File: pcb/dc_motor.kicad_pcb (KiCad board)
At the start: 2 copper layers, 0 parts

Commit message: Sch complete.
first revision.
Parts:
- added C1: 100nF, Capacitor_SMD:C_0603_1608Metric, F.Cu at (147.3, 112.8)
- added C10: 220nF, Capacitor_SMD:C_0603_1608Metric, F.Cu at (143.3, 112.9)
- added C11: 220nF, Capacitor_SMD:C_0603_1608Metric, F.Cu at (146.3, 110.3)
- added C12: 100nF, Capacitor_SMD:C_0603_1608Metric, F.Cu at (175.5, 81.0)
- added C13: 220nF, Capacitor_SMD:C_0603_1608Metric, F.Cu at (171.4, 83.6)
- added C14: 100nF, Capacitor_SMD:C_0603_1608Metric, F.Cu at (143.3, 115.4)
- added C15: 220nF, Capacitor_SMD:C_0603_1608Metric, F.Cu at (172.5, 86.1)
- added C16: 220nF, Capacitor_SMD:C_0603_1608Metric, F.Cu at (175.4, 83.6)
- added C17: 100nF, Capacitor_SMD:C_0603_1608Metric, F.Cu at (155.3, 112.0)
- added C18: 220nF, Capacitor_SMD:C_0603_1608Metric, F.Cu at (139.3, 114.4)
- added C19: 100nF, Capacitor_SMD:C_0603_1608Metric, F.Cu at (147.3, 115.3)
- added C2: 100nF, Capacitor_SMD:C_0603_1608Metric, F.Cu at (176.5, 91.2)
- added C20: 100nF, Capacitor_SMD:C_0603_1608Metric, F.Cu at (179.4, 83.5)
- added C3: 100nF, Capacitor_SMD:C_0603_1608Metric, F.Cu at (164.9, 102.8)
- added C4: 100nF, Capacitor_SMD:C_0603_1608Metric, F.Cu at (168.9, 100.3)
- added C5: 100nF, Capacitor_SMD:C_0603_1608Metric, F.Cu at (173.5, 97.3)
- added C6: 100nF, Capacitor_SMD:C_0603_1608Metric, F.Cu at (151.3, 114.0)
- added C7: 10uF, Capacitor_SMD:C_0805_2012Metric, F.Cu at (165.7, 95.0)
- added C8: 10uF, Capacitor_SMD:C_0805_2012Metric, F.Cu at (171.6, 78.3)
- added C9: 1000uF/35V, Capacitor_THT:CP_Radial_D10.0mm_P5.00mm, F.Cu at (148.1, 94.9)
- added D1: 10V, Diode_SMD:D_SOD-123, F.Cu at (134.4, 114.8)
- added D2: Power, LED_SMD:LED_0603_1608Metric, F.Cu at (142.2, 110.3)
- added D3: RIGTH, LED_SMD:LED_0603_1608Metric, F.Cu at (171.5, 81.1)
- added D4: LEFT, LED_SMD:LED_0603_1608Metric, F.Cu at (175.9, 78.1)
- added FID1: Fiducial, Fiducial:Fiducial_0.5mm_Mask1.5mm, F.Cu at (154.1, 86.3)
- added FID2: Fiducial, Fiducial:Fiducial_0.5mm_Mask1.5mm, F.Cu at (179.4, 78.3)
- added FID3: Fiducial, Fiducial:Fiducial_0.5mm_Mask1.5mm, F.Cu at (164.4, 105.6)
- added FID4: Fiducial, Fiducial:Fiducial_0.5mm_Mask1.5mm, F.Cu at (154.8, 114.7)
- added H1: MountingHole, MountingHole:MountingHole_3.2mm_M3_ISO14580, F.Cu at (151.3, 104.2)
- added H2: MountingHole, MountingHole:MountingHole_3.2mm_M3_ISO14580, F.Cu at (159.9, 95.4)
- added H3: MountingHole, MountingHole:MountingHole_3.2mm_M3_ISO14580, F.Cu at (159.9, 88.3)
- added H4: MountingHole, MountingHole:MountingHole_3.2mm_M3_ISO14580, F.Cu at (167.0, 90.0)
- added J1: Conn_01x02, Connector_Phoenix_MSTB:PhoenixContact_MSTBVA_2,5_2-G-5,08_1x02_P5.08mm_Vertical, F.Cu at (134.9, 95.4)
- added J2: Conn_01x04, Connector_Phoenix_MSTB:PhoenixContact_MSTBVA_2,5_4-G-5,08_1x04_P5.08mm_Vertical, F.Cu at (115.1, 83.0)
- added J3: Conn_01x04, Connector_Molex:Molex_KK-254_AE-6410-04A_1x04_P2.54mm_Vertical, F.Cu at (112.8, 112.0)
- added J4: Conn_01x07, Connector_Molex:Molex_KK-254_AE-6410-07A_1x07_P2.54mm_Vertical, F.Cu at (112.8, 91.8)
- added JP1: SolderJumper_3_Open, Jumper:SolderJumper-3_P1.3mm_Open_RoundedPad1.0x1.5mm, F.Cu at (143.2, 107.0)
- added JP2: EN_Option, Connector_PinHeader_2.54mm:PinHeader_1x03_P2.54mm_Vertical, F.Cu at (167.1, 79.1)
- added Q1: Q_PMOS_GDS, Package_TO_SOT_SMD:TO-252-2, F.Cu at (158.7, 80.8)
- added Q2: BTN8982TA, Package_TO_SOT_SMD:TO-263-7_TabPin8, F.Cu at (119.4, 101.9)
- added Q3: BTN8982TA, Package_TO_SOT_SMD:TO-263-7_TabPin8, F.Cu at (143.8, 82.9)
- added R1: 4k7, Resistor_SMD:R_0603_1608Metric, F.Cu at (172.5, 88.6)
- added R10: 4k7, Resistor_SMD:R_0603_1608Metric, F.Cu at (156.9, 104.4)
- added R11: 3k3, Resistor_SMD:R_0603_1608Metric, F.Cu at (169.9, 94.8)
- added R12: 3k3, Resistor_SMD:R_0603_1608Metric, F.Cu at (156.9, 106.9)
- added R13: 10k, Resistor_SMD:R_0603_1608Metric, F.Cu at (160.9, 102.7)
- added R14: 10k, Resistor_SMD:R_0603_1608Metric, F.Cu at (172.5, 91.2)
- added R15: 10k, Resistor_SMD:R_0603_1608Metric, F.Cu at (151.3, 111.5)
- added R16: 10k, Resistor_SMD:R_0603_1608Metric, F.Cu at (164.9, 100.3)
- added R17: 1k, Resistor_SMD:R_0603_1608Metric, F.Cu at (160.9, 100.2)
- added R18: 1k, Resistor_SMD:R_0603_1608Metric, F.Cu at (176.5, 88.6)
- added R19: 470R, Resistor_SMD:R_0603_1608Metric, F.Cu at (169.5, 97.8)
- added R2: 4k7, Resistor_SMD:R_0603_1608Metric, F.Cu at (176.5, 86.1)
- added R20: 470R, Resistor_SMD:R_0603_1608Metric, F.Cu at (155.3, 109.5)
- added R3: 4k7, Resistor_SMD:R_0603_1608Metric, F.Cu at (165.5, 97.8)
- added R4: 3k3, Resistor_SMD:R_0603_1608Metric, F.Cu at (160.9, 107.7)
- added R5: 10R, Resistor_SMD:R_0603_1608Metric, F.Cu at (173.9, 93.7)
- added R6: 10mR, Resistor_SMD:R_2512_6332Metric, F.Cu at (135.9, 110.7)
- added R7: 10k, Resistor_SMD:R_0603_1608Metric, F.Cu at (160.9, 105.2)
- added R8: 10R, Resistor_SMD:R_0603_1608Metric, F.Cu at (150.3, 109.0)
- added R9: 4k7, Resistor_SMD:R_0603_1608Metric, F.Cu at (156.9, 101.9)
- added U1: L7805, Package_TO_SOT_SMD:TO-252-3_TabPin2, F.Cu at (134.3, 104.2)
- added U2: INA226, Package_SO:VSSOP-10_3x3mm_P0.5mm, F.Cu at (144.1, 102.9)
- added U3: 74AHC244, Package_SO:TSSOP-20_4.4x6.5mm_P0.65mm, F.Cu at (127.1, 112.3)

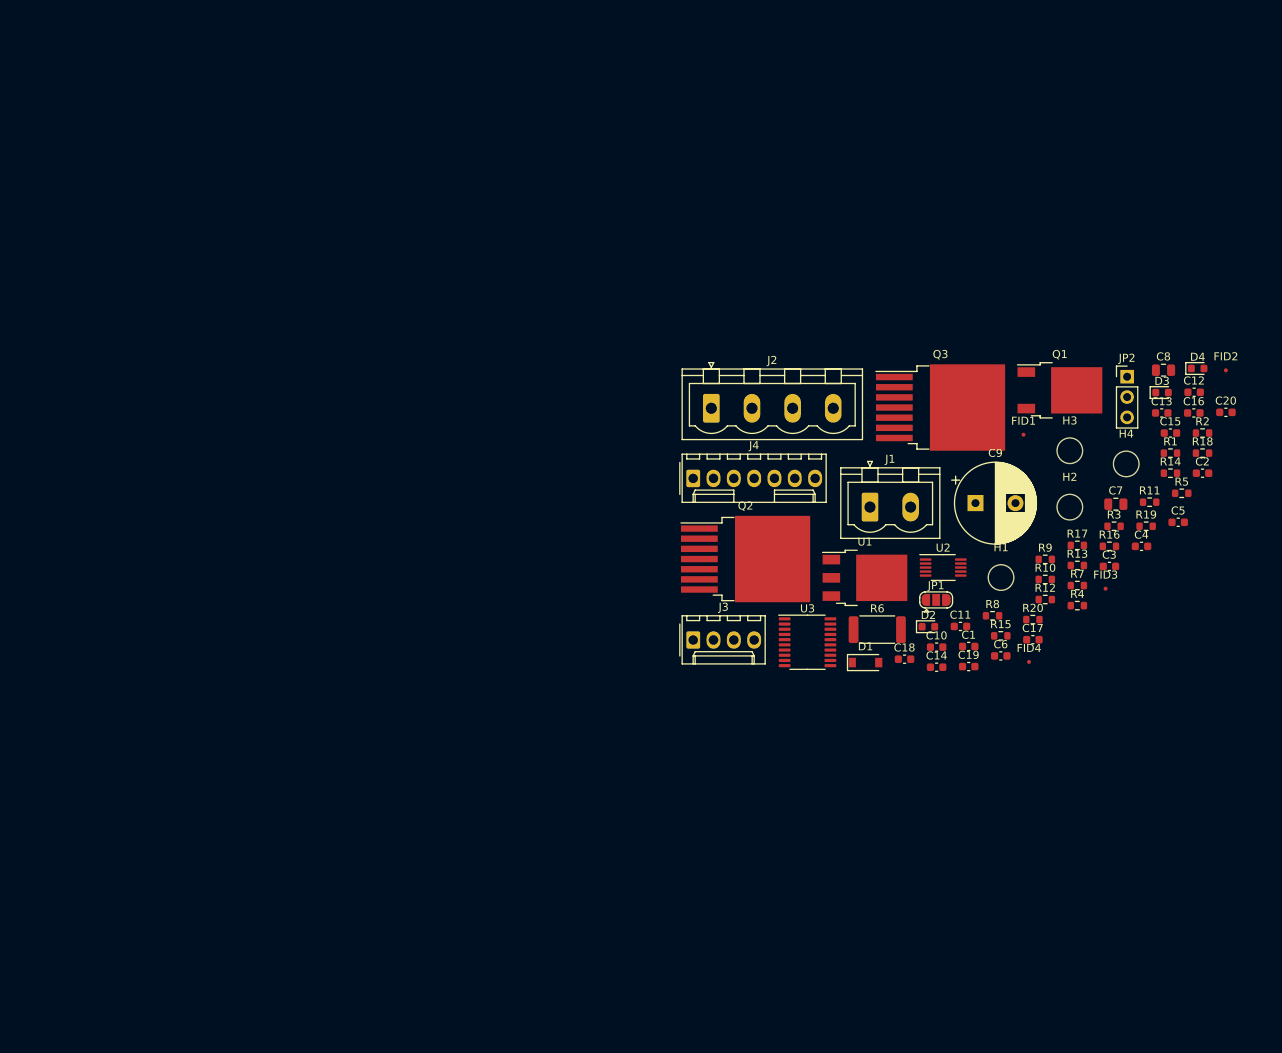
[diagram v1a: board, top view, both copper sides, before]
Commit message: Part number changes
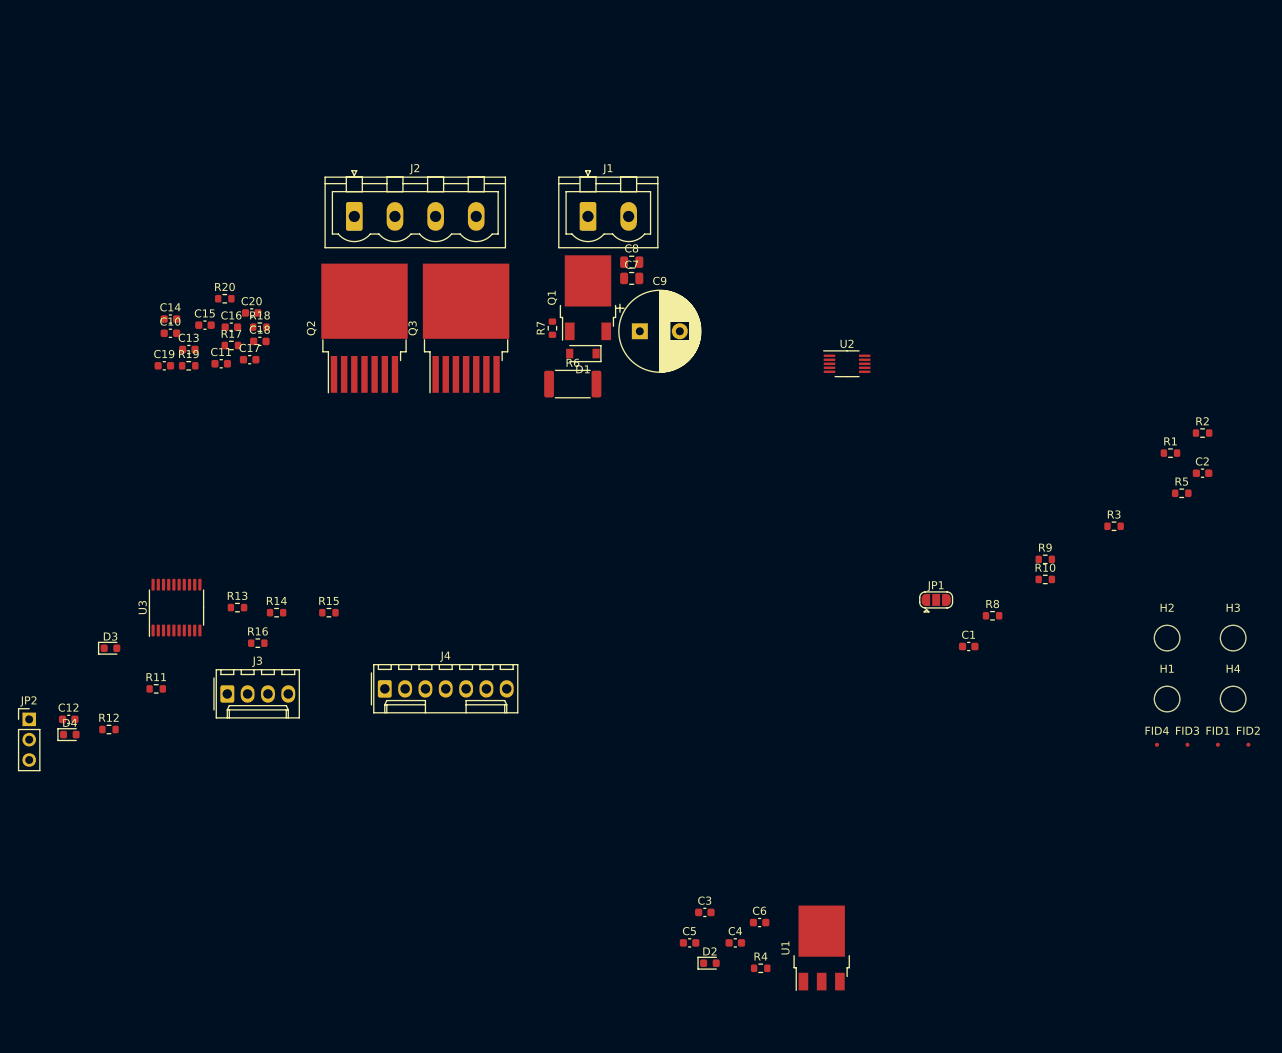
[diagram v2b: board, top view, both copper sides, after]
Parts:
- moved D4 148.2 mm to (34.9, 123.8)
- moved C12 146.5 mm to (34.8, 121.9)
- moved JP2 143.8 mm to (29.8, 121.9)
- moved D3 135.3 mm to (40.0, 113.0)
- moved R11 126.4 mm to (45.7, 118.1)
- moved C20 122.4 mm to (57.7, 71.1)
- moved C13 121.9 mm to (49.8, 75.7)
- moved C15 121.4 mm to (51.8, 72.6)
- moved R19 121.3 mm to (49.8, 77.7)
- moved C16 120.8 mm to (55.1, 72.9)
- moved R18 118.9 mm to (58.7, 72.9)
- moved R12 118.2 mm to (39.8, 123.2)
- moved R14 113.1 mm to (60.8, 108.6)
- moved R20 108.7 mm to (54.3, 69.3)
- moved R17 108.7 mm to (55.1, 75.2)
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
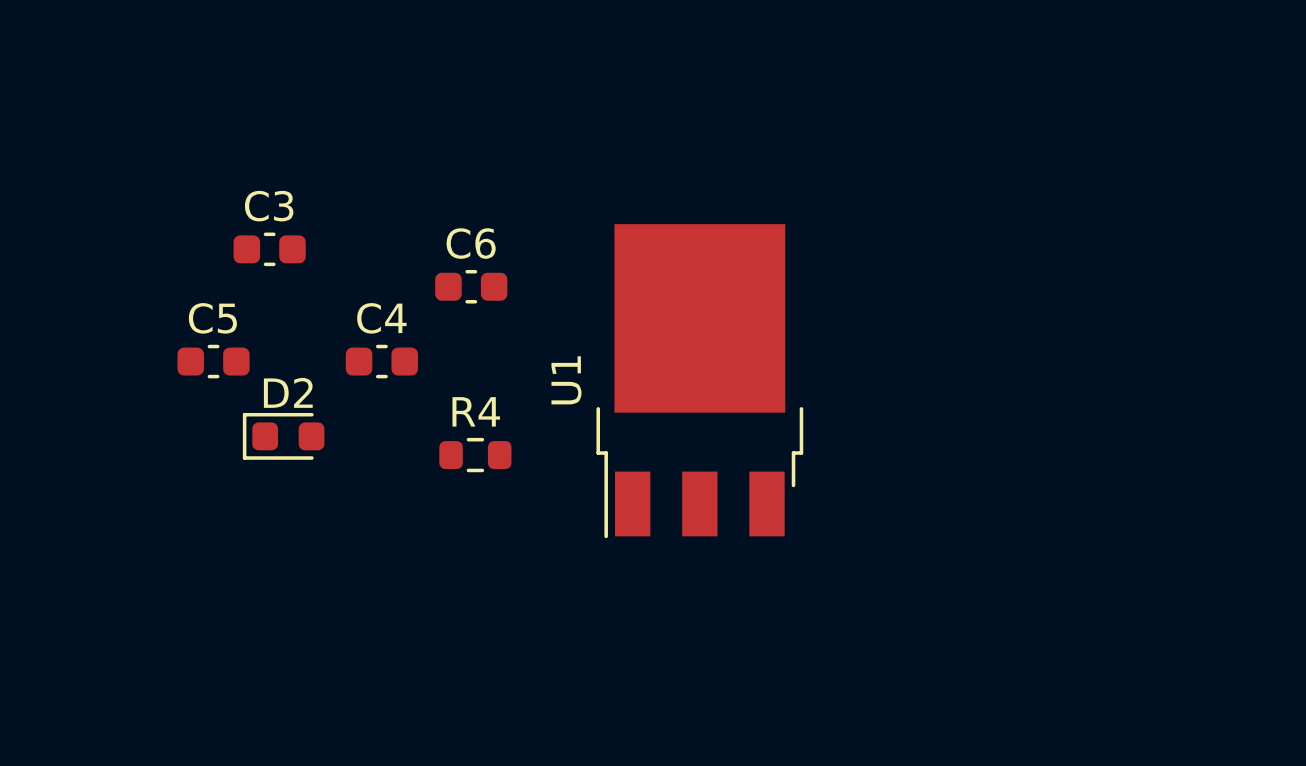
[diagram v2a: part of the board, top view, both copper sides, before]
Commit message: Rev1
Correcciones de primera revisión del profesor, hasta el esquemático.
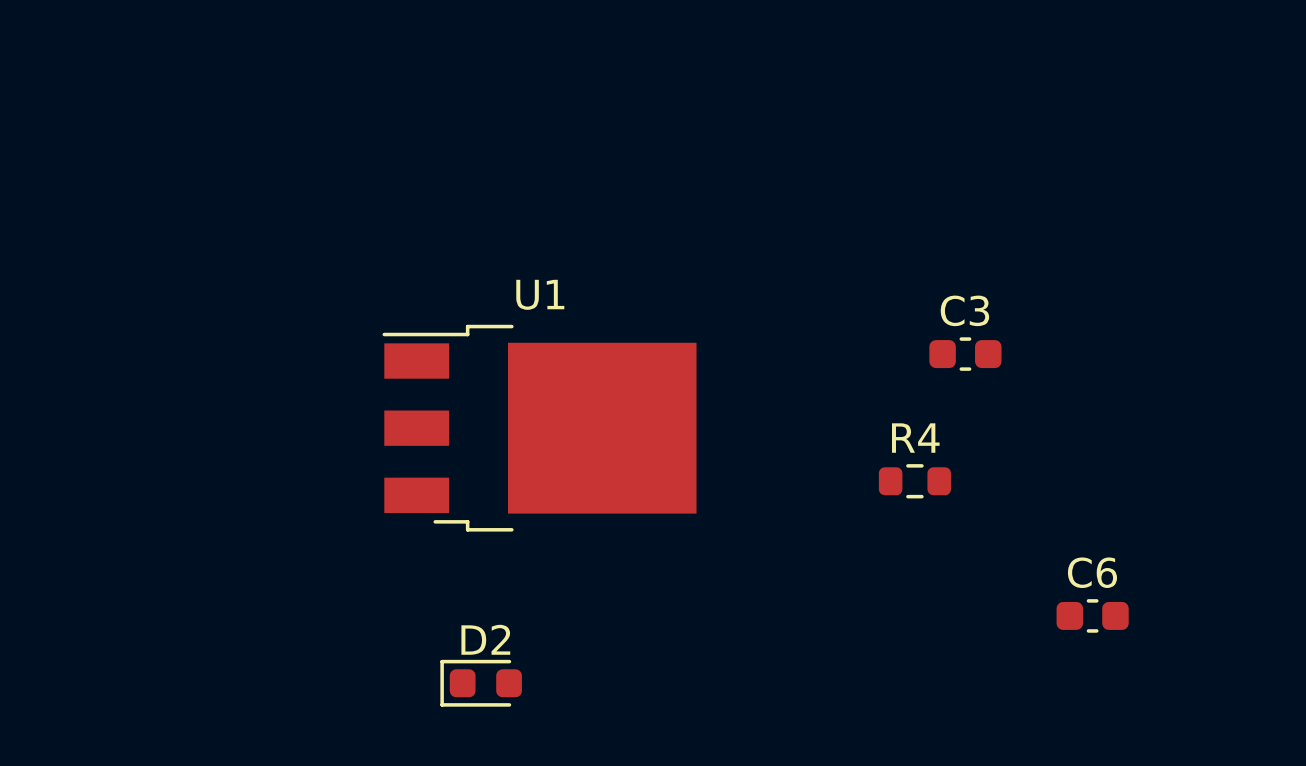
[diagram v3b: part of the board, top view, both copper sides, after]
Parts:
- removed C4, C5: 100nF, Capacitor_SMD:C_0603_1608Metric
- D2: value Power -> Green led 0603
- D3: value RIGTH -> Yellow led 0603
- D4: value LEFT -> Blue led 0603
- Q1: value Q_PMOS_GDS -> IPD90P03P4L04
- moved C3 23.9 mm to (137.9, 149.6)
- moved C6 23.9 mm to (142.2, 158.5)
- moved R4 14.9 mm to (136.2, 153.9)
- moved D2 10.7 mm to (121.6, 160.8)
- moved U1 5.65 mm to (123.5, 152.1), turned to 0 degrees

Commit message: Placement
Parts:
- moved H2 129.7 mm to (54.0, 58.0)
- moved FID4 127.0 mm to (63.0, 58.0)
- moved H1 118.6 mm to (54.0, 108.0)
- moved FID3 118.6 mm to (63.0, 85.0)
- moved FID1 89.5 mm to (114.0, 63.0)
- moved H3 85.4 mm to (114.0, 58.0)
- moved C2 77.6 mm to (99.0, 87.0)
- moved C6 77.3 mm to (108.4, 89.0)
- moved R5 76.2 mm to (98.2, 84.7), turned to 90 degrees
- moved FID2 74.6 mm to (114.0, 95.0)
- moved R2 74.6 mm to (103.2, 99.8), turned to 90 degrees
- moved C3 74.5 mm to (103.9, 83.3), turned to 270 degrees
- moved R1 71.8 mm to (101.6, 99.8), turned to 90 degrees
- moved D2 70.9 mm to (111.5, 90.6), turned to 180 degrees
- moved R4 69.2 mm to (108.4, 90.6), turned to 180 degrees
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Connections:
- J3 pad 1: /SDA -> GND
- J3 pad 2: /SCL -> /ALERT
- J3 pad 3: /ALERT -> /SDA
- J3 pad 4: GND -> /SCL
- J4 pad 2: /PWM2 -> /EN_1
- J4 pad 3: /EN_1 -> /PWM2
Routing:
- net Vdrive: vias 0 -> 18
- net Net-(C20-Pad1): vias 0 -> 1
- net Net-(C19-Pad1): vias 0 -> 1
- net Net-(C11-Pad2): vias 0 -> 37
- net Net-(C10-Pad2): vias 0 -> 38
- net GND: vias 0 -> 17
- net /IS-B: vias 0 -> 1
- net /IS-A: vias 0 -> 1
- net /INH-B: vias 0 -> 1
- net /INH-A: vias 0 -> 1
- net /IN-B: vias 0 -> 1
- net /IN-A: vias 0 -> 1
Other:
- board outline added: 80 x 70 mm

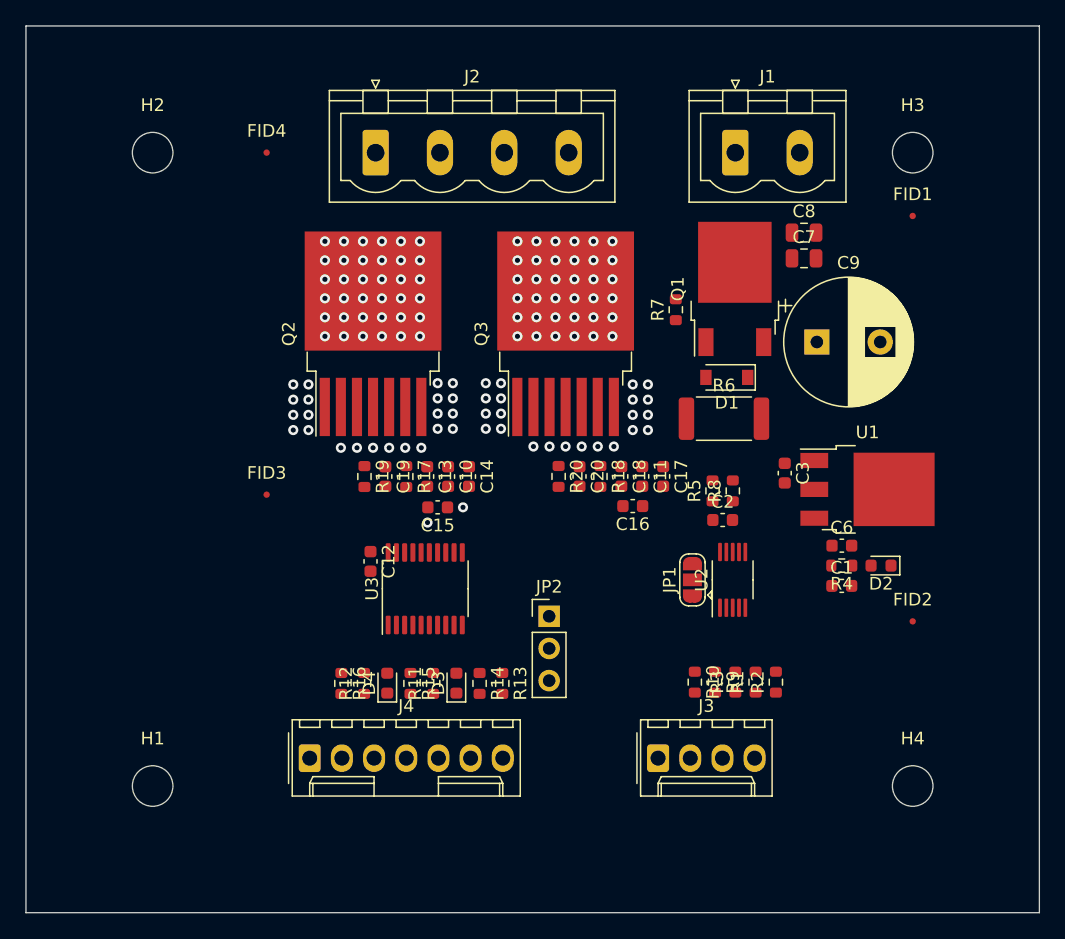
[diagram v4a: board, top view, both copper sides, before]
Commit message: board dimension
change 1 capacitor value.
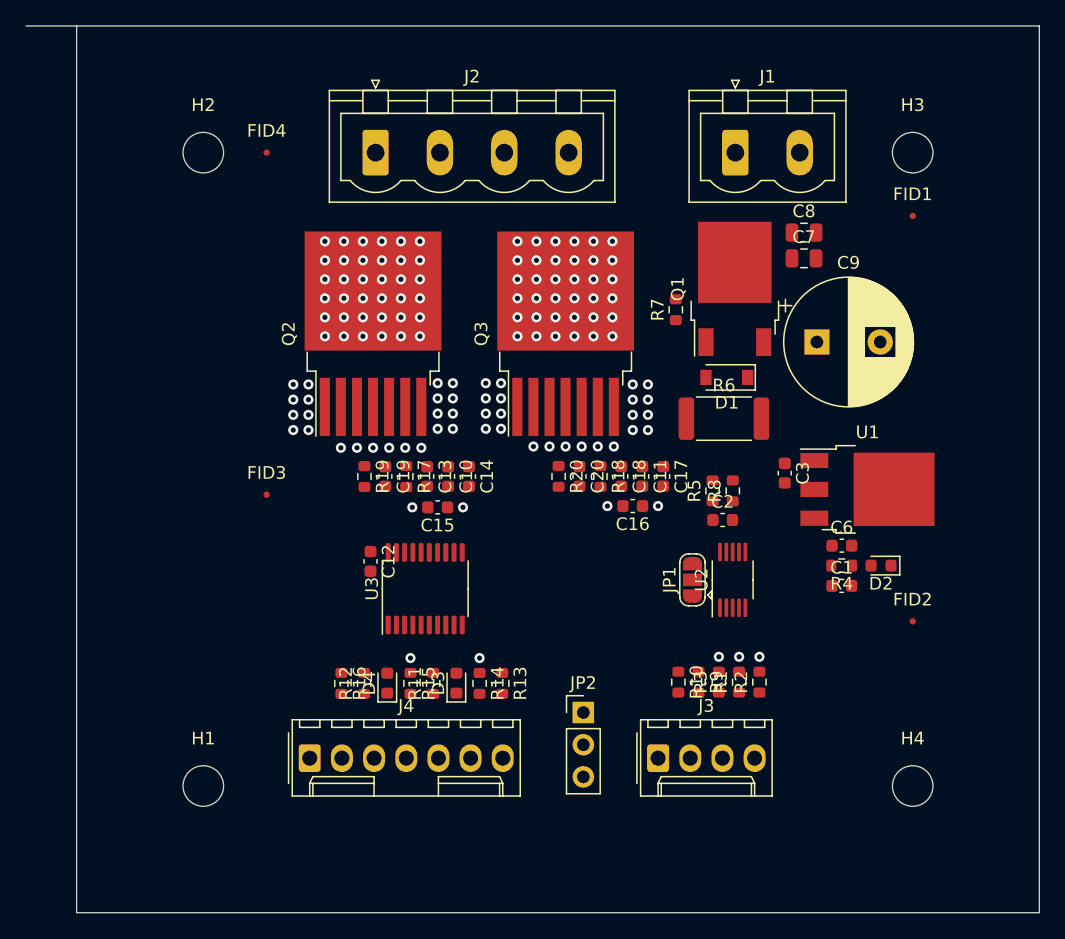
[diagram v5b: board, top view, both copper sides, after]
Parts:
- C13, C18: value 220nF -> 1nF
- moved JP2 8.07 mm to (88.0, 102.2)
- moved H1 4.00 mm to (58.0, 108.0)
- moved H2 4.00 mm to (58.0, 58.0)
- moved R9 1.30 mm to (97.1, 99.8)
- moved R1 1.30 mm to (100.3, 99.8)
- moved R10 1.30 mm to (95.5, 99.8)
- moved R2 1.30 mm to (101.9, 99.8)
- moved R3 1.30 mm to (98.7, 99.8)
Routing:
- net Net-(C11-Pad2): vias 37 -> 38
- net GND: vias 17 -> 18
- net /SDA: vias 0 -> 1
- net /SCL: vias 0 -> 1
- net /PWM2: vias 0 -> 1
- net /EN_1: vias 0 -> 1
- net /ALERT: vias 0 -> 1
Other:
- outline, holes or cut-outs redrawn
